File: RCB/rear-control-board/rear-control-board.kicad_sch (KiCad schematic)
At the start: 11 parts, among them J1 Conn_01x23, J2 Conn_01x23, J3 Conn_01x08, K1 T9VV1K15-12S, U3 LDL1117S33R

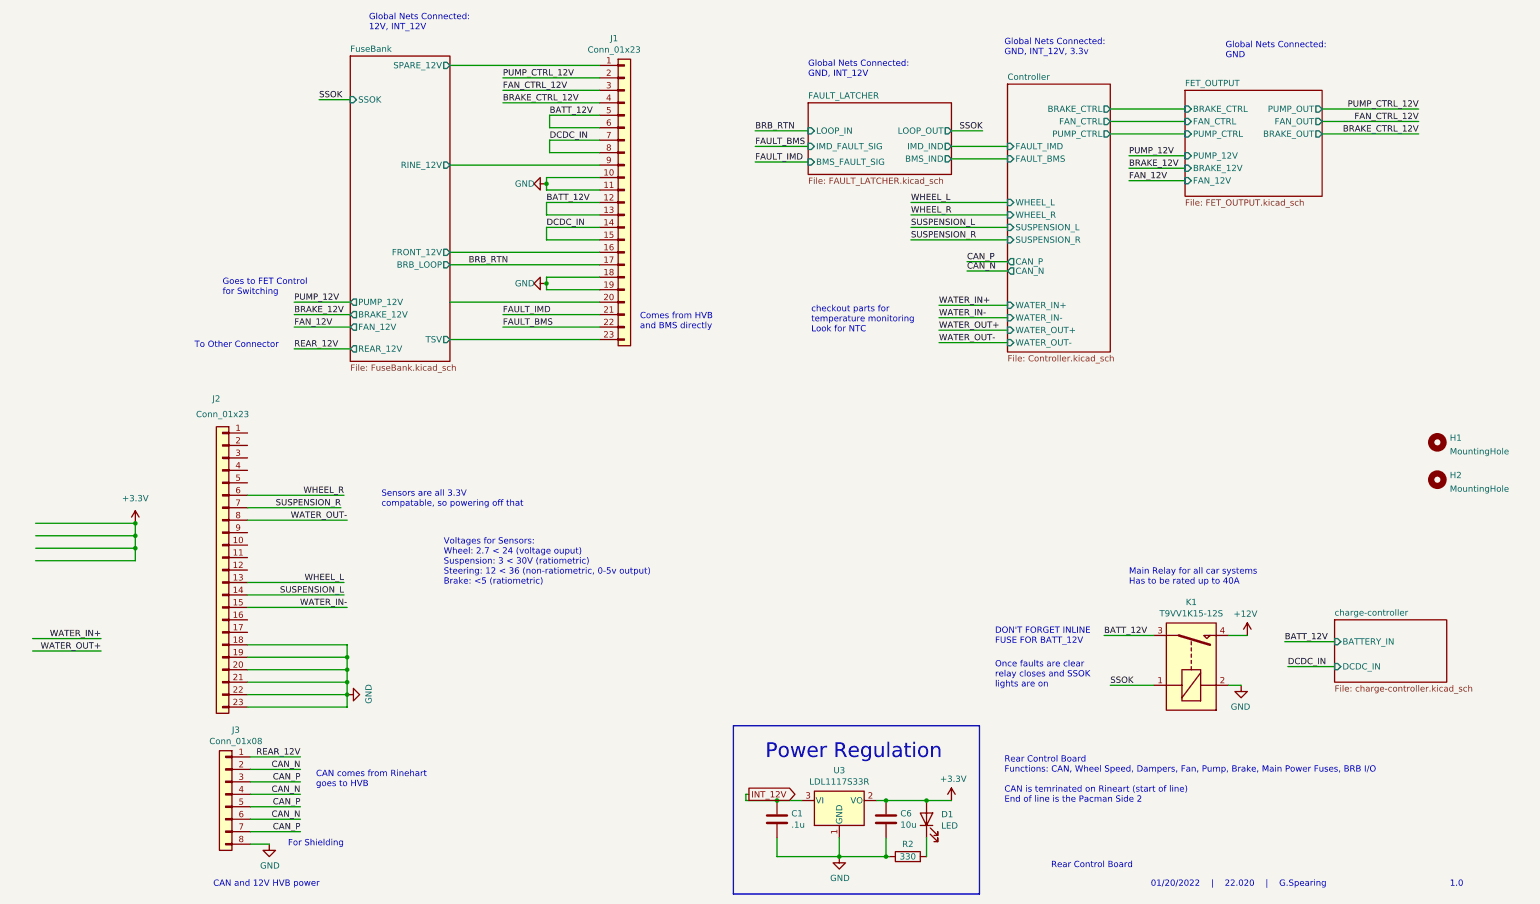
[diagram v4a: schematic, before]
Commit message: updating layout with schem changes
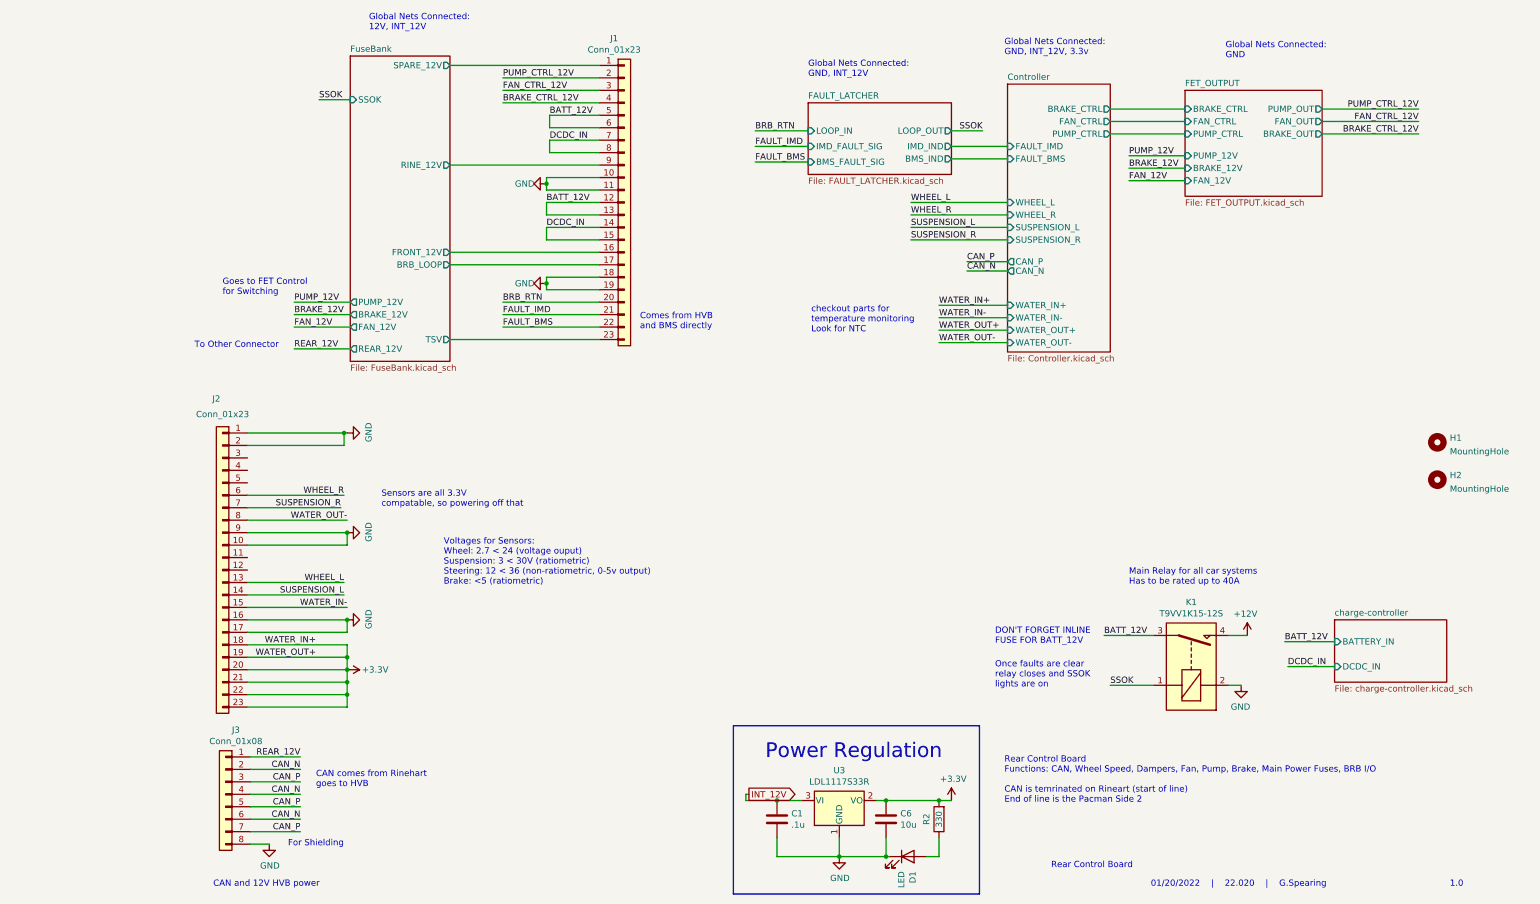
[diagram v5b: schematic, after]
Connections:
- net +3V3: now also J2.18 (Pin_18), J2.19 (Pin_19), J2.20 (Pin_20), J2.21 (Pin_21), J2.22 (Pin_22), J2.23 (Pin_23), R2.2; no longer D1.2 (A)
- net BRB_RTN: now also J1.20 (Pin_20); no longer J1.17 (Pin_17)
- net GND: now also D1.1 (K), J2.1 (Pin_1), J2.10 (Pin_10), J2.16 (Pin_16), J2.17 (Pin_17), J2.2 (Pin_2), J2.9 (Pin_9); no longer J2.18 (Pin_18), J2.19 (Pin_19), J2.20 (Pin_20), J2.21 (Pin_21), J2.22 (Pin_22), J2.23 (Pin_23), R2.1
- new net: D1.2 (A), R2.1
- new net FuseBank/BRB_LOOP: J1.17 (Pin_17)
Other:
- moved on the sheet: D1, R2

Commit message: touching up layout and making gerbers
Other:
- note added: "Rear Control Board Functions: CAN, Wheel Speed, Dampers, Fan, Pump, Brake, Main Power Fuses, BRB I/O - CAN from rinehart to HVB CAN is temrinated on Rineart (start of line) End of line is the Pacman Side 2"
- note removed: "Rear Control Board Functions: CAN, Wheel Speed, Dampers, Fan, Pump, Brake, Main Power Fuses, BRB I/O CAN is temrinated on Rineart (start of line) End of line is the Pacman Side 2"
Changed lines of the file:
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@@
     (effects (font (size 1.27 1.27)) (justify left bottom))
   )
-  (text "Rear Control Board\nFunctions: CAN, Wheel Speed, Dampers, Fan, Pump, Brake, Main Power Fuses, BRB I/O\n\nCAN is temrinated on Rineart (start of line)\nEnd of line is the Pacman Side 2"
+  (text "Rear Control Board\nFunctions: CAN, Wheel Speed, Dampers, Fan, Pump, Brake, Main Power Fuses, BRB I/O\n- CAN from rinehart to HVB\nCAN is temrinated on Rineart (start of line)\nEnd of line is the Pacman Side 2"
     (at 178.435 177.165 0)
     (effects (font (size 1.27 1.27)) (justify left bottom))

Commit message: Addded comments
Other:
- note added: "BMS"
- note added: "BRB_RTN"
- note added: "DCB"
- note added: "Footprint is wrong not far enough horizontal hits board edge"
- note added: "GND to sensors"
- note added: "Ground to Frame"
- note added: "HVB not rinehart"
- note added: "NOT SSOK"
- note added: "When BRB is open no pwr when closed turns on relay"
- note added: "to HVB"
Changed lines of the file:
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@@
     (effects (font (size 1.27 1.27)) (justify left bottom))
+  )
+  (text "HVB not rinehart\n" (at 57.15 168.91 0)
+    (effects (font (size 1.27 1.27) bold italic) (justify left bottom))
   )
   (text "Main Relay for all car systems\nHas to be rated up to 40A"
@@
     (effects (font (size 1.27 1.27)) (justify left bottom))
   )
+  (text "Footprint is wrong not far \nenough horizontal hits board edge"
+    (at 26.67 97.79 0)
+    (effects (font (size 1.27 1.27) bold italic) (justify left bottom))
+  )
   (text "checkout parts for \ntemperature monitoring\nLook for NTC"
     (at 139.065 81.28 0)
     (effects (font (size 1.27 1.27)) (justify left bottom))
   )
+  (text "When BRB is open\nno pwr when\nclosed turns on relay"
+    (at 169.545 135.89 0)
+    (effects (font (size 1.27 1.27) (thickness 0.254) bold italic) (justify left bottom))
+  )
   (text "Global Nets Connected: \nGND, INT_12V" (at 138.43 29.21 0)
     (effects (font (size 1.27 1.27)) (justify left bottom))
@@
     (effects (font (size 1.27 1.27)) (justify left bottom))
   )
+  (text "GND to sensors" (at 15.875 145.415 90)
+    (effects (font (size 1.27 1.27) bold italic) (justify left bottom))
+  )
   (text "DON'T FORGET INLINE \nFUSE FOR BATT_12V" (at 176.53 144.78 0)
     (effects (font (size 1.27 1.27)) (justify left bottom))
   )
+  (text "NOT SSOK" (at 198.755 158.75 0)
+    (effects (font (size 1.27 1.27) bold italic) (justify left bottom))
+  )
   (text "01/20/2022    |    22.020    |    G.Spearing" (at 208.28 194.31 0)
     (effects (font (size 1.27 1.27)) (justify left bottom))
+  )
+  (text "DCB" (at 56.515 63.5 0)
+    (effects (font (size 1.27 1.27) bold italic) (justify left bottom))
   )
   (text "CAN and 12V HVB power" (at 17.145 194.31 0)
@@
     (effects (font (size 1.27 1.27)) (justify left bottom))
   )
+  (text "BMS" (at 67.31 26.67 0)
+    (effects (font (size 1.27 1.27) bold italic) (justify left bottom))
+  )
+  (text "Ground to Frame" (at 102.87 52.07 0)
+    (effects (font (size 1.27 1.27) bold italic) (justify left bottom))
+  )
   (text "To Other Connector" (at 13.335 84.455 0)
     (effects (font (size 1.27 1.27)) (justify left bottom))
@@
   (text "For Shielding" (at 32.385 186.055 0)
     (effects (font (size 1.27 1.27)) (justify left bottom))
+  )
+  (text "BRB_RTN\n" (at 199.39 156.21 0)
+    (effects (font (size 1.27 1.27) bold italic) (justify left bottom))
   )
   (text "Power Regulation" (at 165.735 168.275 180)
@@
   (text "Global Nets Connected: \nGND, INT_12V, 3.3v" (at 178.435 24.765 0)
     (effects (font (size 1.27 1.27)) (justify left bottom))
+  )
+  (text "to HVB" (at 35.56 165.735 0)
+    (effects (font (size 1.27 1.27) bold italic) (justify left bottom))
   )
   (text "Sensors are all 3.3V\ncompatable, so powering off that"
@@
       (reference "#PWR0153") (unit 1) (value "GND") (footprint "")
     )
+    (path "/00000000-0000-0000-0000-000061f4d99a/1c46d95b-6e65-4538-beaf-c69ab0281a72"
+      (reference "#PWR?") (unit 1) (value "GND") (footprint "")
+    )
+    (path "/00000000-0000-0000-0000-000062054c3a/2bc736be-1609-4140-b513-c7de4eddc976"
+      (reference "#PWR?") (unit 1) (value "+3.3V") (footprint "")
+    )
+    (path "/00000000-0000-0000-0000-000062054c3a/42c5f480-cc28-4207-9dcf-d4c24e1c4fd6"
+      (reference "#PWR?") (unit 1) (value "GND") (footprint "")
+    )
     (path "/43c66bc4-7c60-4b3c-9292-9f929454c596"
       (reference "C1") (unit 1) (value ".1u") (footprint "Capacitor_SMD:C_0603_1608Metric_Pad1.08x0.95mm_HandSolder")
@@
       (reference "K3") (unit 1) (value "G5V-2") (footprint "Relay_THT:Relay_DPDT_Omron_G5V-2")
     )
+    (path "/00000000-0000-0000-0000-000062054c3a/3e3338cf-cf80-4af8-88b2-56ae48f97e0d"
+      (reference "Q?") (unit 1) (value "B5584") (footprint "Package_TO_SOT_SMD:SOT-363_SC-70-6")
+    )
     (path "/00000000-0000-0000-0000-000061f4d99a/324c0c76-58ea-4deb-ae27-182fa8148008"
       (reference "R1") (unit 1) (value "20k") (footprint "Resistor_SMD:R_0603_1608Metric_Pad0.98x0.95mm_HandSolder")
@@
       (reference "R17") (unit 1) (value "200k") (footprint "Resistor_SMD:R_0603_1608Metric_Pad0.98x0.95mm_HandSolder")
     )
+    (path "/00000000-0000-0000-0000-000061f4d99a/9adcaaf9-3cec-4a35-9baa-c1374c92a7f2"
+      (reference "R?") (unit 1) (value "10k") (footprint "")
+    )
+    (path "/00000000-0000-0000-0000-000062054c3a/ec4b0bef-8187-4d99-b62c-b559b50cd5f8"
+      (reference "R?") (unit 1) (value "470") (footprint "")
+    )
     (path "/00000000-0000-0000-0000-000061ef11ea/00000000-0000-0000-0000-0000618b3473"
